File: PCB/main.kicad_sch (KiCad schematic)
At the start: 61 parts, among them J1 S20B-PADSS-1, J2 S20B-PADSS-1, J3 SWD, SW1 SPST, U1 TPS5430, U2 AMS1117-3.3, U3 MCP2558FD, U4 MCP2558FD, U5 STM32G0B1, Y1 ${Frequency}

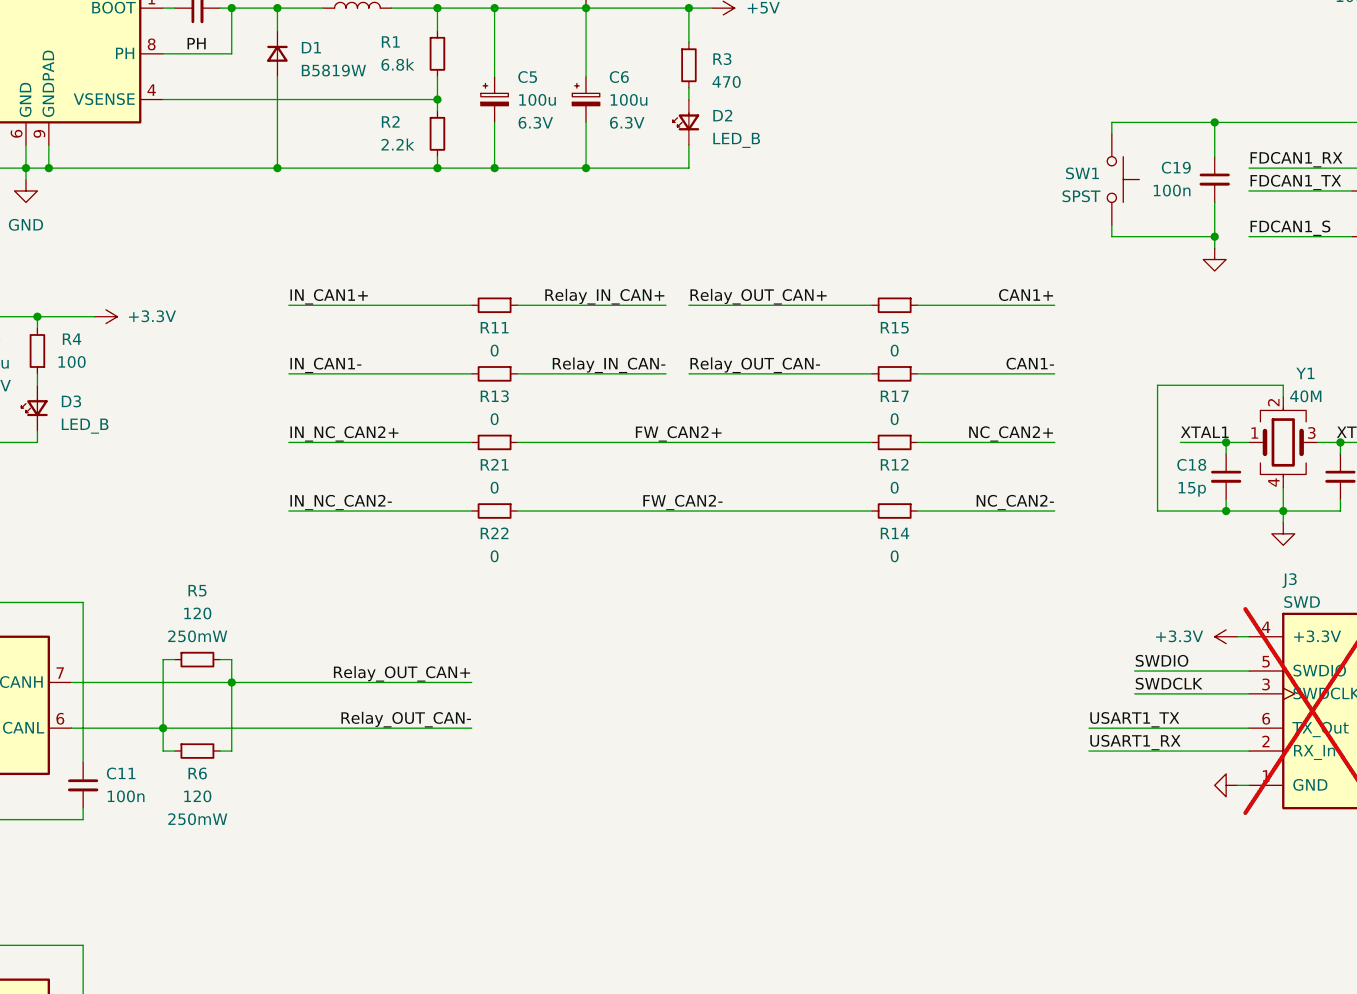
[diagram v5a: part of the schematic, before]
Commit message: Switch to multi library parts system
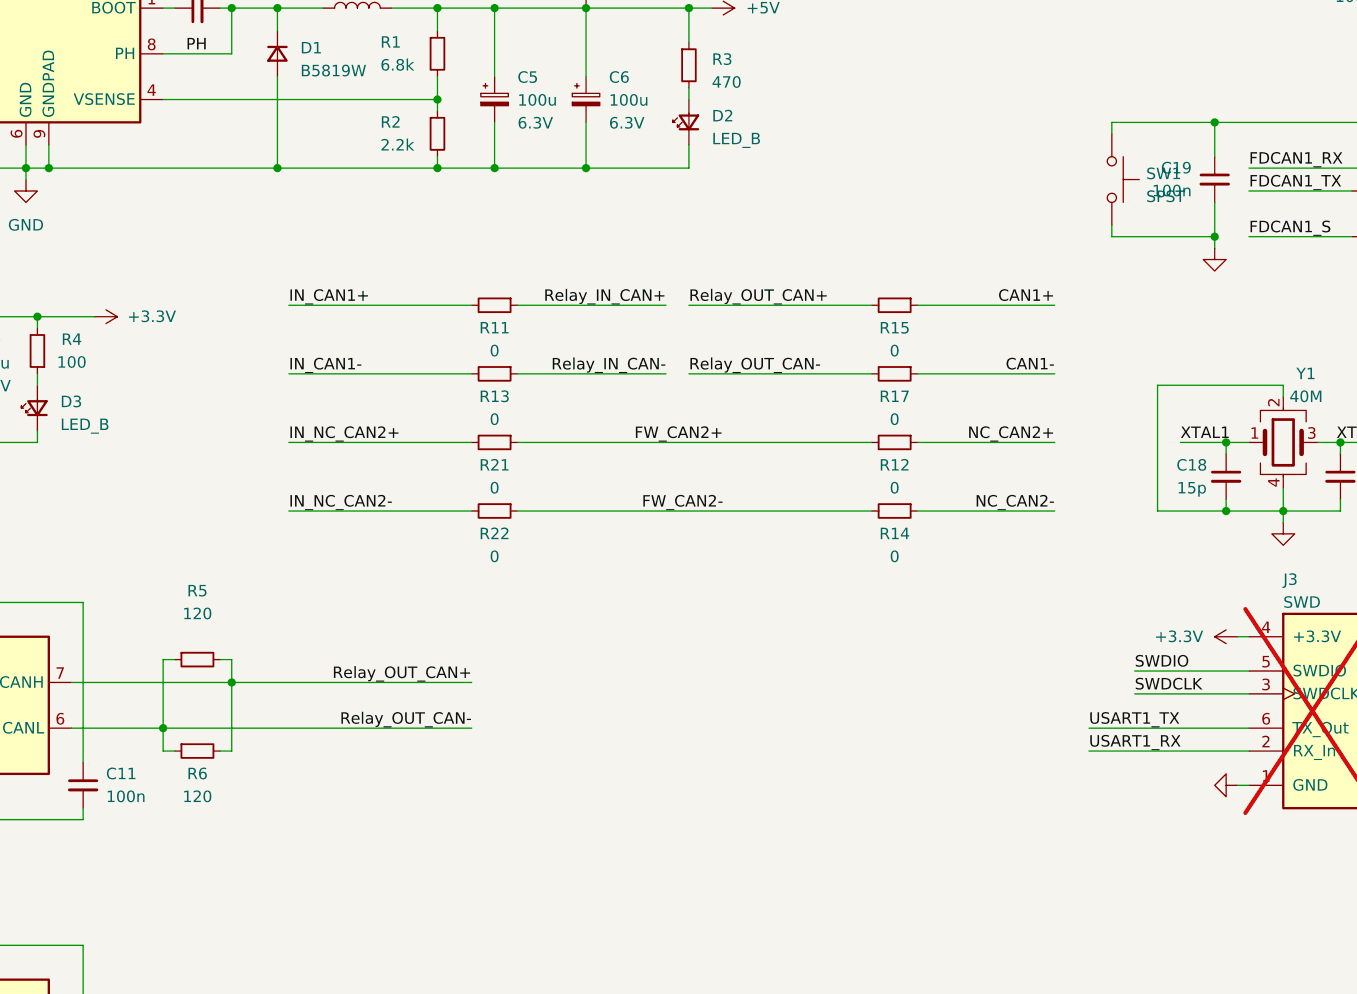
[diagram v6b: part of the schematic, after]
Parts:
- ART1: symbol 0 LibDB:Artwork/CMP-0044 -> 0 Other:Artwork/CMP-0044
- ART2: symbol 0 LibDB:Artwork/CMP-0045 -> 0 Other:Artwork/CMP-0045
- ART3: symbol 0 LibDB:Artwork/CMP-0047 -> 0 Other:Artwork/CMP-0047
- C1, C2, C7, C8, C9: symbol 0 LibDB:Capacitors/CMP-0029 -> 0 Passive_Components:Capacitors/CMP-0029
- C10, C11, C12, C13: symbol 0 LibDB:Capacitors/CMP-0021 -> 0 Passive_Components:Capacitors/CMP-0021
- C14: symbol 0 LibDB:Capacitors/CMP-0051 -> 0 Passive_Components:Capacitors/CMP-0051
- C15, C16, C19: symbol 0 LibDB:Capacitors/CMP-0049 -> 0 Passive_Components:Capacitors/CMP-0049
- C17, C18: symbol 0 LibDB:Capacitors/CMP-0005 -> 0 Passive_Components:Capacitors/CMP-0005
- C3: symbol 0 LibDB:Capacitors/CMP-0031 -> 0 Passive_Components:Capacitors/CMP-0031
- C4: symbol 0 LibDB:Capacitors/CMP-0032 -> 0 Passive_Components:Capacitors/CMP-0032
- C5, C6: symbol 0 LibDB:Capacitors/CMP-0017 -> 0 Passive_Components:Capacitors/CMP-0017
- D1: symbol 0 LibDB:Schottky Diodes/CMP-0033 -> 0 Diodes:Schottky Diodes/CMP-0033
- D2, D3, D4: symbol 0 LibDB:LEDs/CMP-0023 -> 0 Opto_Electronics:LEDs/CMP-0023
- F1: symbol 0 LibDB:Circuit Protection/CMP-0026 -> 0 Circuit_Protection:Fuse Holders/CMP-0026
- J1, J2: symbol 0 LibDB:Connectors/CMP-0012 -> 0 Connectors:Headers & Wire Housings/CMP-0012
- J3: symbol 0 LibDB:Connectors/CMP-0053 -> 0 Connectors:Headers & Wire Housings/CMP-0053
- L1: symbol 0 LibDB:Inductors/CMP-0036 -> 0 Passive_Components:Inductors/CMP-0036
- R1: symbol 0 LibDB:Resistors/CMP-0034 -> 0 Passive_Components:Resistors/CMP-0034
- R10, R8: symbol 0 LibDB:Resistors/CMP-0010 -> 0 Passive_Components:Resistors/CMP-0010
- R11, R12, R13, R14, R15, R17, R21, R22, R23, R24, R25, R26, R7, R9: symbol 0 LibDB:Resistors/CMP-0007 -> 0 Passive_Components:Resistors/CMP-0007
- R2: symbol 0 LibDB:Resistors/CMP-0035 -> 0 Passive_Components:Resistors/CMP-0035
- R27, R4: symbol 0 LibDB:Resistors/CMP-0024 -> 0 Passive_Components:Resistors/CMP-0024
- R3: symbol 0 LibDB:Resistors/CMP-0037 -> 0 Passive_Components:Resistors/CMP-0037
- R5, R6: symbol 0 LibDB:Resistors/CMP-0006 -> 0 Passive_Components:Resistors/CMP-0006
- SW1: symbol 0 LibDB:Switches/CMP-0011 -> 0 Electromechanical:Tactile Switches/CMP-0011
- U1: symbol 0 LibDB:DC-DC Converters/CMP-0030 -> 0 Power_Management:Buck Regulators/CMP-0030
- U2: symbol 0 LibDB:LDO Regulators/CMP-0027 -> 0 Power_Management:LDO Regulators/CMP-0027
- U3, U4: symbol 0 LibDB:ICs/CMP-0002 -> 0 Interfaces:CAN Tranceivers/CMP-0002
- U5: symbol 0 LibDB:ICs/CMP-0003 -> 0 MCUs_Processors:Arm Cortex M0/CMP-0003
- Y1: symbol 0 LibDB:Crystals/CMP-0004 -> 0 Passive_Components:Crystals/CMP-0004

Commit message: Start moving to TPS54302
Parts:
- added C20, C22, C25, C26: ${Capacitance}, Capacitor_SMD:C_1206_3216Metric, symbol 0 Passive_Components:Capacitors/CMP-0031
- added C23: ${Capacitance}, Capacitor_SMD:C_0402_1005Metric, symbol 0 Passive_Components:Capacitors/CMP-0049
- added C24: ${Capacitance}, Capacitor_SMD:C_0402_1005Metric, symbol 0 Passive_Components:Capacitors/CMP-0057
- added D5: LED_B, LED_SMD:LED_0603_1608Metric, symbol 0 Opto_Electronics:LEDs/CMP-0023
- added L2: ${Inductance}, libdb:CMP-0058, symbol 0 Passive_Components:Inductors/CMP-0058
- added R16: ${Resistance}, Resistor_SMD:R_0402_1005Metric, symbol 0 Passive_Components:Resistors/CMP-0055
- added R18: ${Resistance}, Resistor_SMD:R_0402_1005Metric, symbol 0 Passive_Components:Resistors/CMP-0056
- added R19: ${Resistance}, Resistor_SMD:R_0402_1005Metric, symbol 0 Passive_Components:Resistors/CMP-0037
- added R20: ${Resistance}, Resistor_SMD:R_0402_1005Metric, symbol 0 Passive_Components:Resistors/CMP-0060
- added R28: ${Resistance}, Resistor_SMD:R_0402_1005Metric, symbol 0 Passive_Components:Resistors/CMP-0061
- added U6: TPS54302, Package_TO_SOT_SMD:SOT-23-6, symbol 0 Power_Management:Buck Regulators/CMP-0054
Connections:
- net +5V: now also C24.1, C25.1, C26.1, L2.2, R19.1, R28.1; no longer C5.1, C6.1, L1.2, R1.1, R3.1
- net +BATT: now also C20.1, C22.1, R16.1, U6.3 (VIN)
- net GND: now also C20.2, C22.2, C25.2, C26.2, D5.1 (K), R18.2, R20.2, U6.1 (GND)
- new net: C5.1, C6.1, L1.2, R1.1, R3.1
- new net: R16.2, R18.1, U6.5 (EN)
- new net: C24.2, R20.1, R28.2, U6.4 (FB)
- new net: D5.2 (A), R19.2
- new net: C23.2, L2.1, U6.2 (SW)
- new net: C23.1, U6.6 (BOOT)
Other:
- note added: "UVLO VSTART=8V VSTOP=7V RH = 512552R = 510k RL = 87594R = 100k VSTART=7.08V VSTOP=6.11V"
- moved on the sheet: C1, C2, C3, C4, C5, C6, D1, D2, L1, R1, R2, R3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

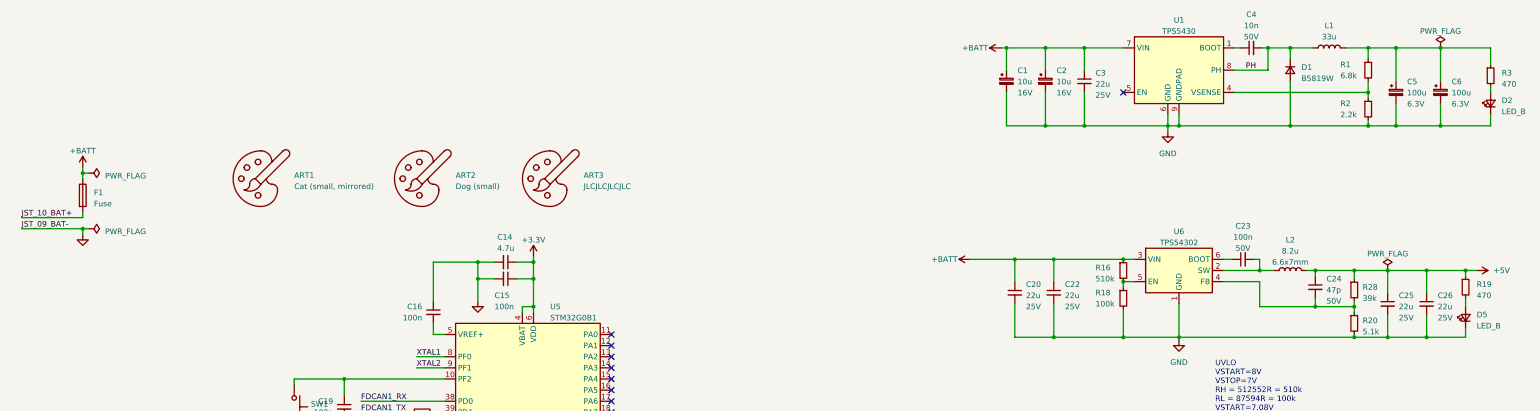
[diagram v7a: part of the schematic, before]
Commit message: Re-layout with TPS54302
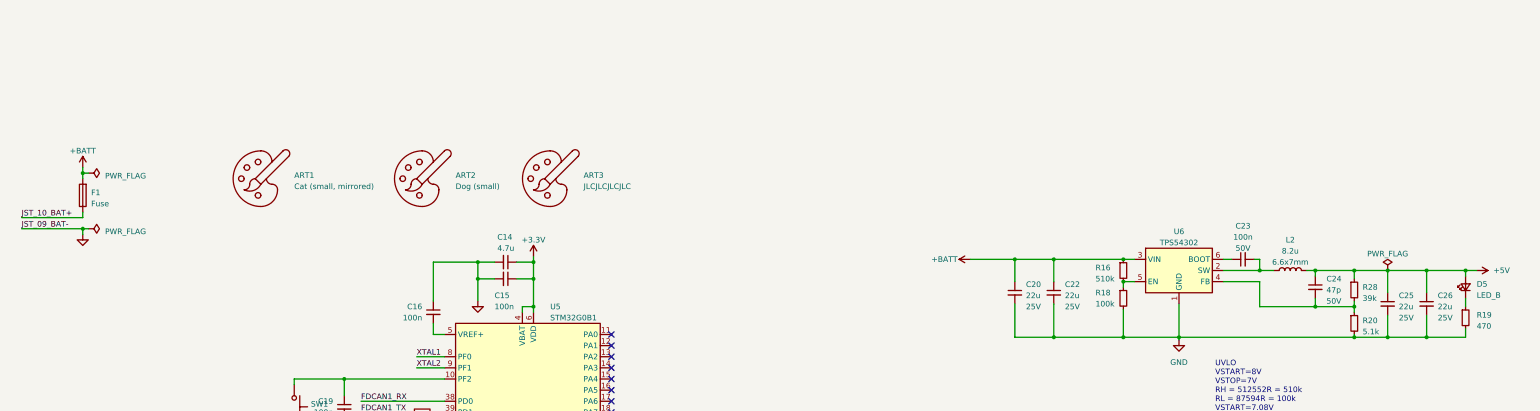
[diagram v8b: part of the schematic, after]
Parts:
- removed C1, C2: ${Capacitance}, Capacitor_Tantalum_SMD:CP_EIA-3216-18_Kemet-A, symbol 0 Passive_Components:Capacitors/CMP-0029
- removed C3: ${Capacitance}, Capacitor_SMD:C_1206_3216Metric, symbol 0 Passive_Components:Capacitors/CMP-0031
- removed C4: ${Capacitance}, Capacitor_SMD:C_0402_1005Metric, symbol 0 Passive_Components:Capacitors/CMP-0032
- removed C5, C6: ${Capacitance}, Capacitor_Tantalum_SMD:CP_EIA-3528-15_AVX-H, symbol 0 Passive_Components:Capacitors/CMP-0017
- removed D1: B5819W, Diode_SMD:D_SOD-123, symbol 0 Diodes:Schottky Diodes/CMP-0033
- removed D2: LED_B, LED_SMD:LED_0603_1608Metric, symbol 0 Opto_Electronics:LEDs/CMP-0023
- removed L1: ${Inductance}, libdb:CMP-0036, symbol 0 Passive_Components:Inductors/CMP-0036
- removed R1: ${Resistance}, Resistor_SMD:R_0402_1005Metric, symbol 0 Passive_Components:Resistors/CMP-0034
- removed R2: ${Resistance}, Resistor_SMD:R_0402_1005Metric, symbol 0 Passive_Components:Resistors/CMP-0035
- removed R3: ${Resistance}, Resistor_SMD:R_0402_1005Metric, symbol 0 Passive_Components:Resistors/CMP-0037
- removed U1: TPS5430, libdb:CMP-0030, symbol 0 Power_Management:Buck Regulators/CMP-0030
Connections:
- net +5V: now also D5.2 (A); no longer R19.1
- net +BATT: now also F1.2; no longer F1.1
- net GND: now also R19.2; no longer D5.1 (K)
- net JST_10_BAT+: now also F1.1; no longer F1.2
- new net: D5.1 (K), R19.1
- no-connect marks 31 -> 30
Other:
- moved on the sheet: D5, F1, R19
